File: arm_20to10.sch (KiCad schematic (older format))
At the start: 10 parts, among them J1 SFH11-PBPC-D10-RA-BK, J2 20021111-00010T4LF, SW1 SSSS810701, U1 MIC5504-3.3YM5 TR

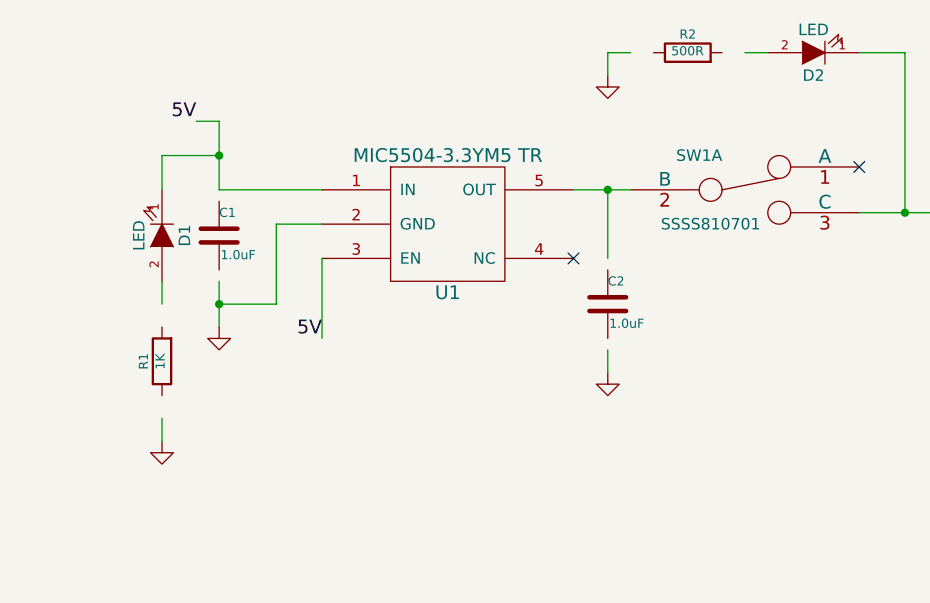
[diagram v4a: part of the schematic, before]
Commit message: try to add some models
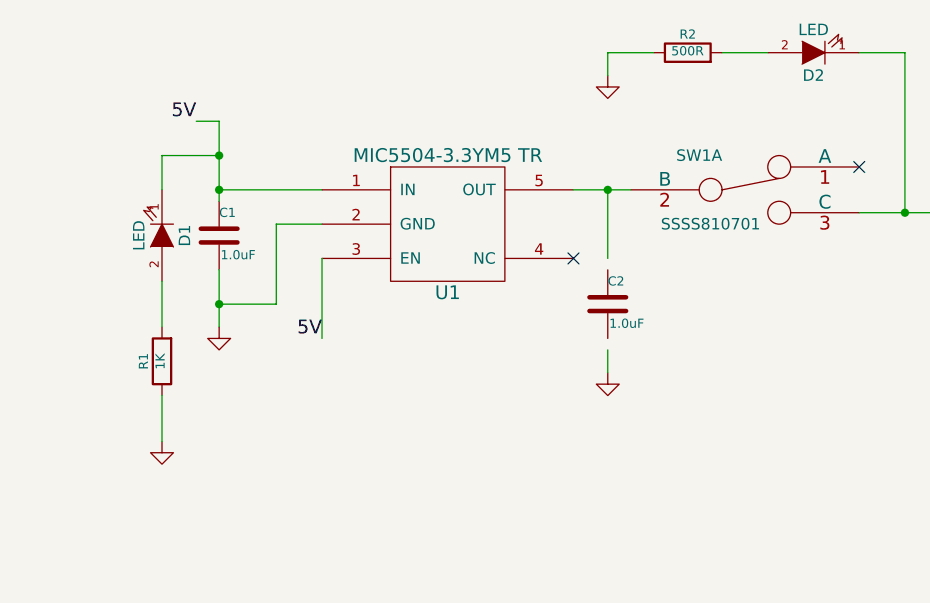
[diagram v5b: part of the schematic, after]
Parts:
- C1, C2: footprint SMD_Packages:SMD-0603_c -> kicadlib:SMD_0603_C
- D1, D2: footprint SMD_Packages:SMD-0603 -> kicadlib:SMD_0603_LED
- R1, R2: footprint SMD_Packages:SMD-0603_r -> kicadlib:SMD_0603_R
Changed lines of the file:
@@
 F 0 "C2" H 8550 2300 40  0000 L CNN
 F 1 "1.0uF" H 8556 2115 40  0000 L CNN
-F 2 "SMD_Packages:SMD-0603_c" H 8588 2050 30  0001 C CNN
+F 2 "kicadlib:SMD_0603_C" H 8588 2050 30  0001 C CNN
 F 3 "~" H 8550 2200 60  0000 C CNN
 	1    8550 2200
@@
 	6750 1400 6850 1400
 Wire Wire Line
-	6850 1400 6850 1700
+	6850 1400 6850 1750
 Wire Wire Line
 	6850 1700 7300 1700
@@
 	7100 1850 7300 1850
 Wire Wire Line
-	6850 2100 6850 2300
+	6850 2050 6850 2300
 Wire Wire Line
 	7100 2200 6850 2200
@@
 F 0 "D2" H 9450 1200 50  0000 C CNN
 F 1 "LED" H 9450 1000 50  0000 C CNN
-F 2 "SMD_Packages:SMD-0603" H 9450 1100 60  0001 C CNN
+F 2 "kicadlib:SMD_0603_LED" H 9450 1100 60  0001 C CNN
 F 3 "~" H 9450 1100 60  0000 C CNN
 	1    9450 1100
@@
 F 0 "R2" V 8980 1100 40  0000 C CNN
 F 1 "500R" V 8907 1101 40  0000 C CNN
-F 2 "SMD_Packages:SMD-0603_r" V 8830 1100 30  0001 C CNN
+F 2 "kicadlib:SMD_0603_R" V 8830 1100 30  0001 C CNN
 F 3 "~" H 8900 1100 30  0000 C CNN
 	1    8900 1100
@@
 $EndComp
 Wire Wire Line
-	8650 1100 8550 1100
+	8550 1100 8750 1100
 Wire Wire Line
 	8550 1100 8550 1200
@@
 $EndComp
 Wire Wire Line
-	9250 1100 9150 1100
+	9050 1100 9250 1100
 $Comp
 L LED D1
@@
 F 0 "D1" H 6600 2000 50  0000 C CNN
 F 1 "LED" H 6600 1800 50  0000 C CNN
-F 2 "SMD_Packages:SMD-0603" H 6600 1900 60  0001 C CNN
+F 2 "kicadlib:SMD_0603_LED" H 6600 1900 60  0001 C CNN
 F 3 "~" H 6600 1900 60  0000 C CNN
 	1    6600 1900
@@
 F 0 "R1" V 6680 2450 40  0000 C CNN
 F 1 "1K" V 6607 2451 40  0000 C CNN
-F 2 "SMD_Packages:SMD-0603_r" V 6530 2450 30  0001 C CNN
+F 2 "kicadlib:SMD_0603_R" V 6530 2450 30  0001 C CNN
 F 3 "~" H 6600 2450 30  0000 C CNN
 	1    6600 2450
@@
 $EndComp
 Wire Wire Line
-	6600 2700 6600 2800
-Wire Wire Line
-	6600 2100 6600 2200
+	6600 2600 6600 2800
+Wire Wire Line
+	6600 2100 6600 2300
 Wire Wire Line
 	6600 1700 6600 1550
@@
 F 0 "C1" H 6850 2000 40  0000 L CNN
 F 1 "1.0uF" H 6856 1815 40  0000 L CNN
-F 2 "SMD_Packages:SMD-0603_c" H 6888 1750 30  0001 C CNN
+F 2 "kicadlib:SMD_0603_C" H 6888 1750 30  0001 C CNN
 F 3 "~" H 6850 1900 60  0000 C CNN
 	1    6850 1900
@@
 Text Label 5950 5100 2    60   ~ 0
 NRST
+Connection ~ 6850 1700
 $EndSCHEMATC
